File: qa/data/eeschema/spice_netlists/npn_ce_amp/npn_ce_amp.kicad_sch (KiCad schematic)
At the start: 10 parts, among them Q1 QNPN

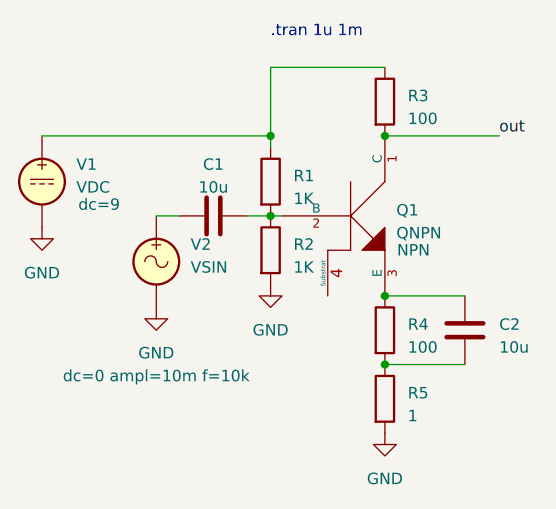
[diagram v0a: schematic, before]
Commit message: Make sim QA tests compare result vectors, not netlist text
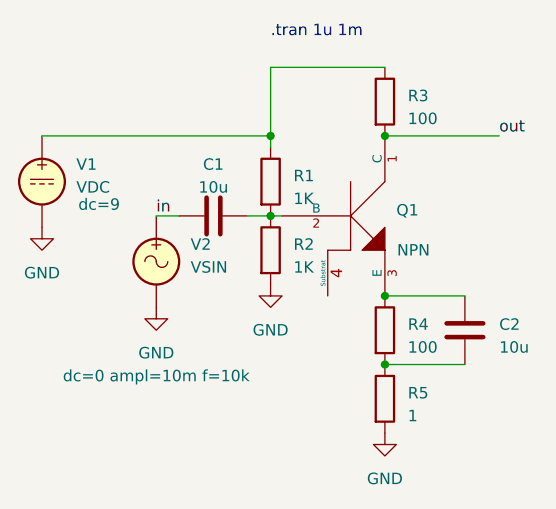
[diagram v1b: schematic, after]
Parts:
- Q1: value QNPN -> (none); Model_Library npn.lib -> npn.lib.spice
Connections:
- net in: now reaches C1.1, V2.1
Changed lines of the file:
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@@
+    (effects (font (size 1.27 1.27)) (justify left bottom))
+  )
+  (label "in" (at 114.3 88.9 0) (fields_autoplaced)
     (effects (font (size 1.27 1.27)) (justify left bottom))
   )
@@
       (effects (font (size 1.27 1.27)) (justify left))
     )
-    (property "Value" "QNPN" (id 1) (at 140.97 90.805 0)
+    (property "Value" "" (id 1) (at 140.97 90.805 0)
       (effects (font (size 1.27 1.27)) (justify left))
     )
@@
       (effects (font (size 1.27 1.27)))
     )
-    (property "Model_Library" "npn.lib" (id 5) (at 135.89 88.9 0)
+    (property "Model_Library" "npn.lib.spice" (id 5) (at 135.89 88.9 0)
       (effects (font (size 1.27 1.27)) hide)
     )
